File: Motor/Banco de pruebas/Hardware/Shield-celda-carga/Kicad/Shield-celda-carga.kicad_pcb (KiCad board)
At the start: 2 copper layers, 54.6 x 49.5 mm, 15 parts, among them J1 Conexion bateria, J2 Screw_Terminal_01x03, J3 Conn_01x04, J4 Alimentacion Arduino, K1 Rele 12V-360mW, Q1 BC337

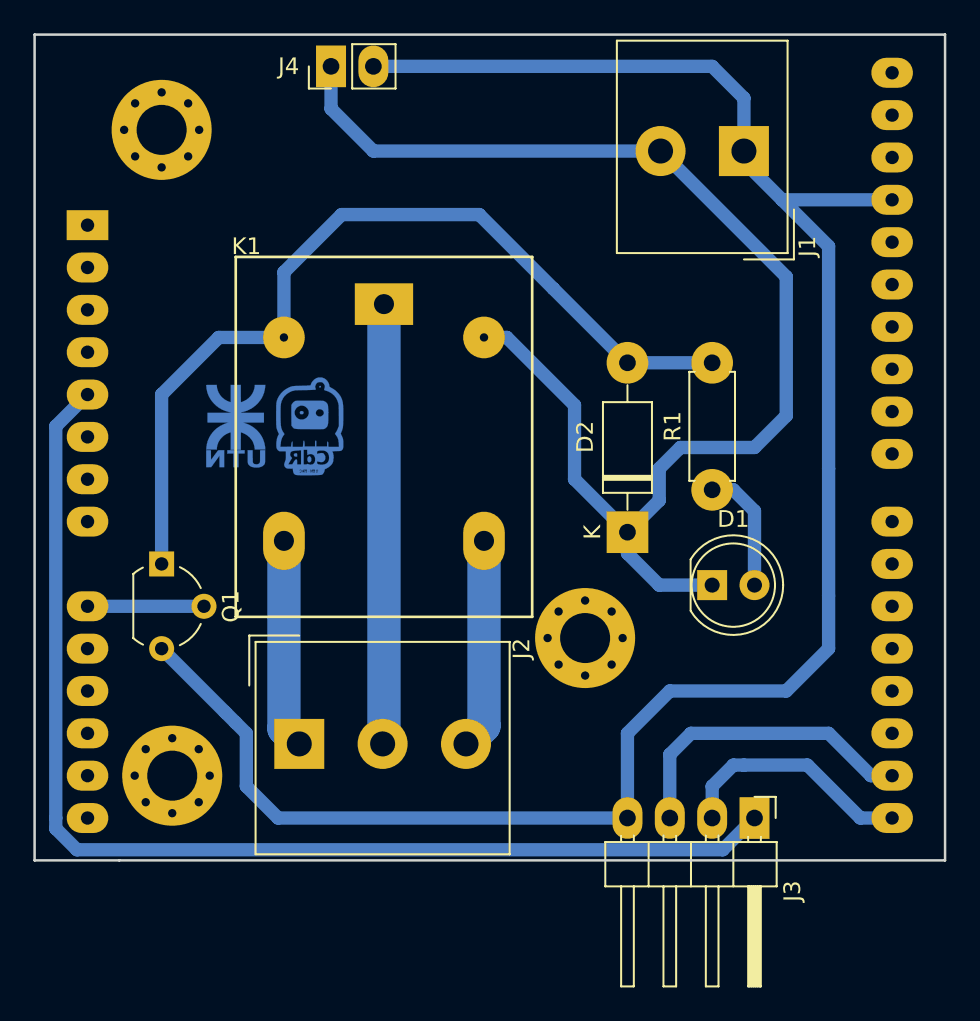
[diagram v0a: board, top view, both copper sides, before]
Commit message: se modifico shiel-celda-carga la distribucion de pines
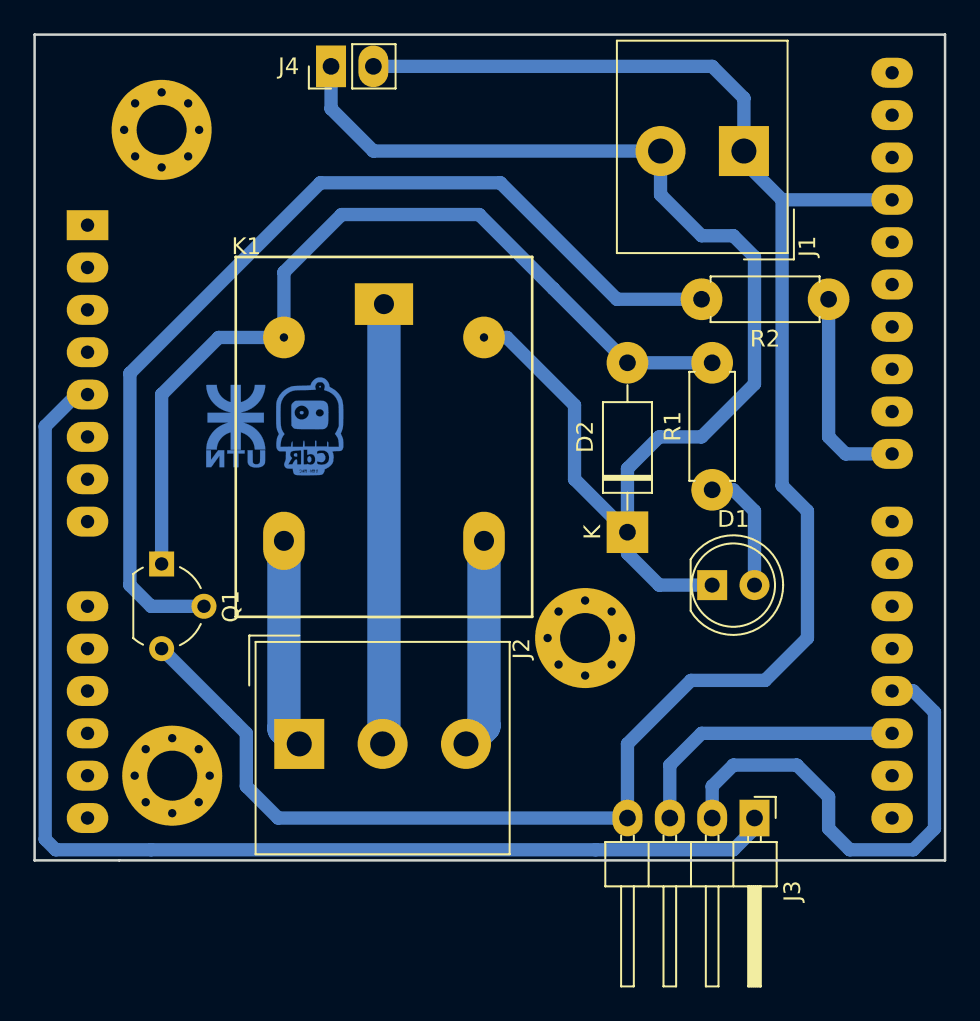
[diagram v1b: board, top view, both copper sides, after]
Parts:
- added R2: 560, Resistor_THT:R_Axial_DIN0207_L6.3mm_D2.5mm_P7.62mm_Horizontal, F.Cu at (76.8, 58.4)
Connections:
- net /VCC renamed /+5V
- A1 pad 15: /SCK -> Net-(A1-Pad15)
- A1 pad 16: /DT -> Net-(A1-Pad16)
- A1 pad 17: Net-(A1-Pad17) -> /DT
- A1 pad 18: Net-(A1-Pad18) -> /SCK
- Q1 pad 2: Net-(A1-Pad9) -> Net-(Q1-Pad2)
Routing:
- net Net-(Q1-Pad2): track 0.00 -> 59.6 mm
- net /SCK: track 14.5 -> 29.6 mm
- net Net-(A1-Pad23): track 0.00 -> 12.5 mm
- net Net-(A1-Pad9): track 6.98 -> 0.00 mm
- net GND: track 118.0 -> 115.5 mm
- net /+5V: track 70.0 -> 72.1 mm
- net +12V: track 79.1 -> 77.5 mm
- net /DT: track 18.7 -> 17.3 mm
